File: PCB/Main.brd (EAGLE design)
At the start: 73 x 61 mm, 4 parts, among them U1 ESP32DEVKITC

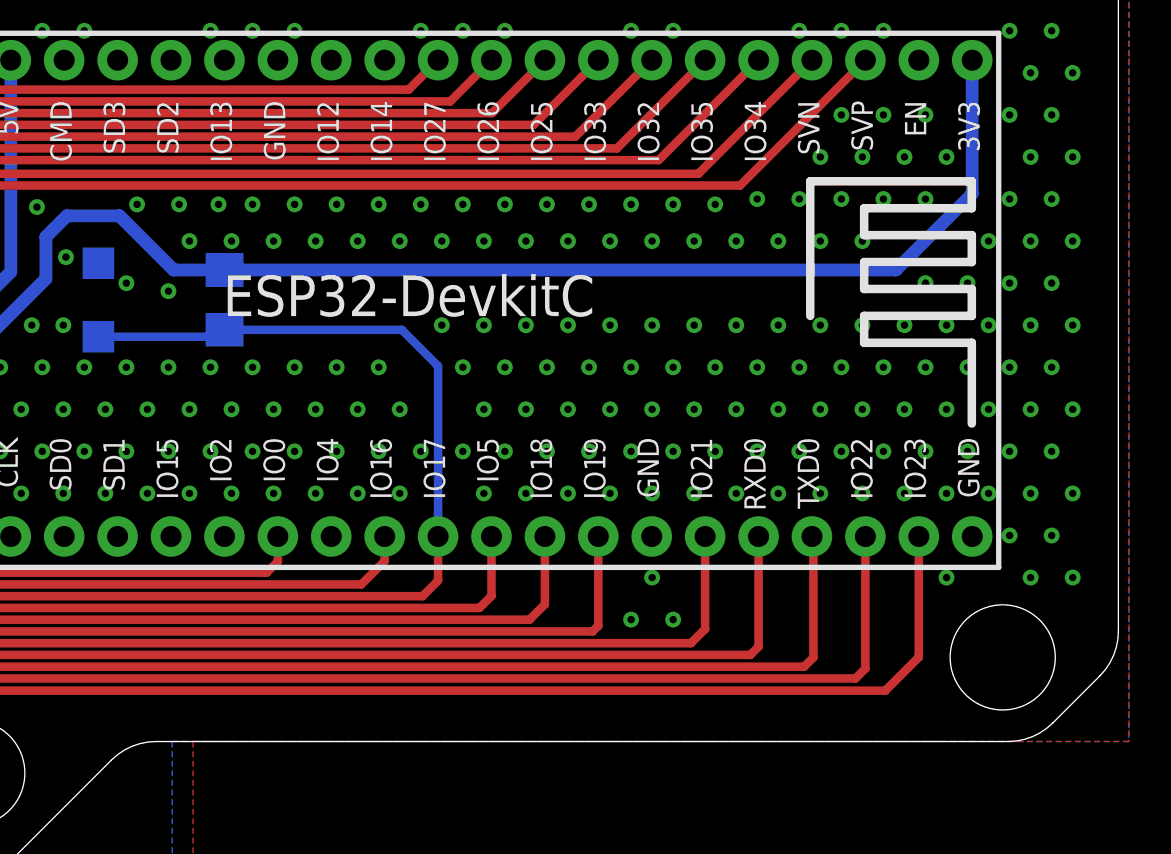
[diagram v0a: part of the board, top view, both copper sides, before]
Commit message: PCB Updates/New Additions
All existing PCBs had silkscreen updates and NES, Virtual Boy, PSX/PS2, Nintendo 64, Saturn have been added.
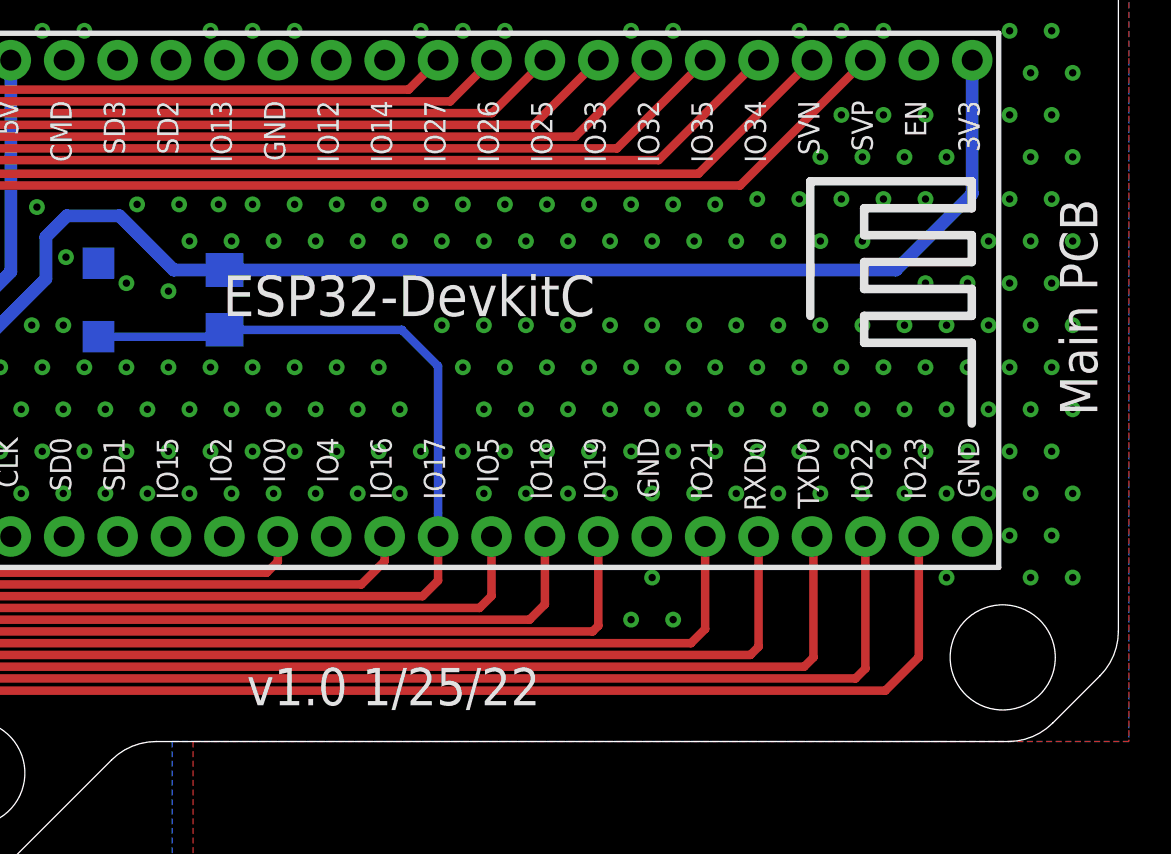
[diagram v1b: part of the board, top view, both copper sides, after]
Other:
- board text added: "Main PCB"
- board text added: "v1.0 1/25/22"
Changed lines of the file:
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@@
 <hole x="18.5" y="53" drill="5"/>
 <hole x="18.5" y="8" drill="5"/>
+<text x="72" y="25" size="1.778" layer="21" rot="R90">Main PCB</text>
+<text x="45.5" y="13" size="1.778" layer="21" rot="R180">v1.0 1/25/22</text>
 </plain>
 <attributes>

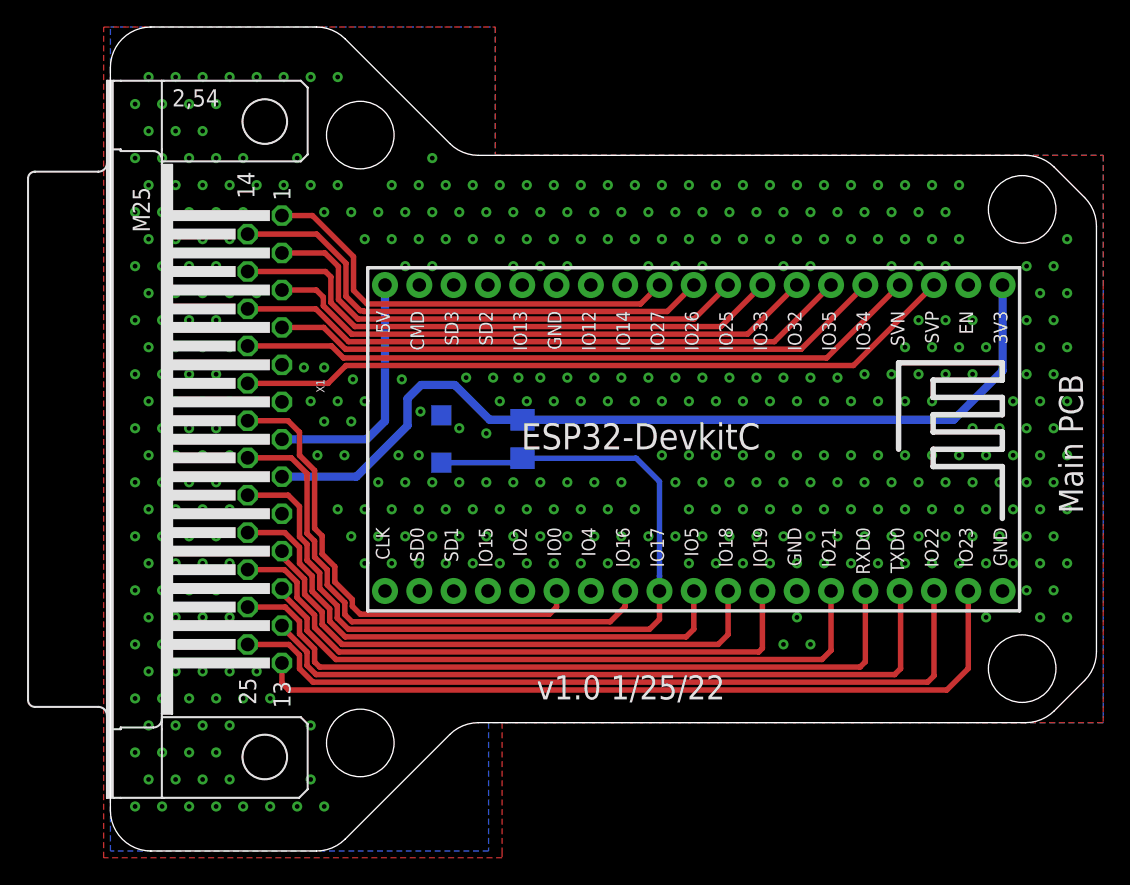
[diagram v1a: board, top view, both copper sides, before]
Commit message: Added exposed GND plane at DB25 anchors
All PCBs have been update to have exposed GND plane pads for the DB25 anchor points.

This resolves Issue 54
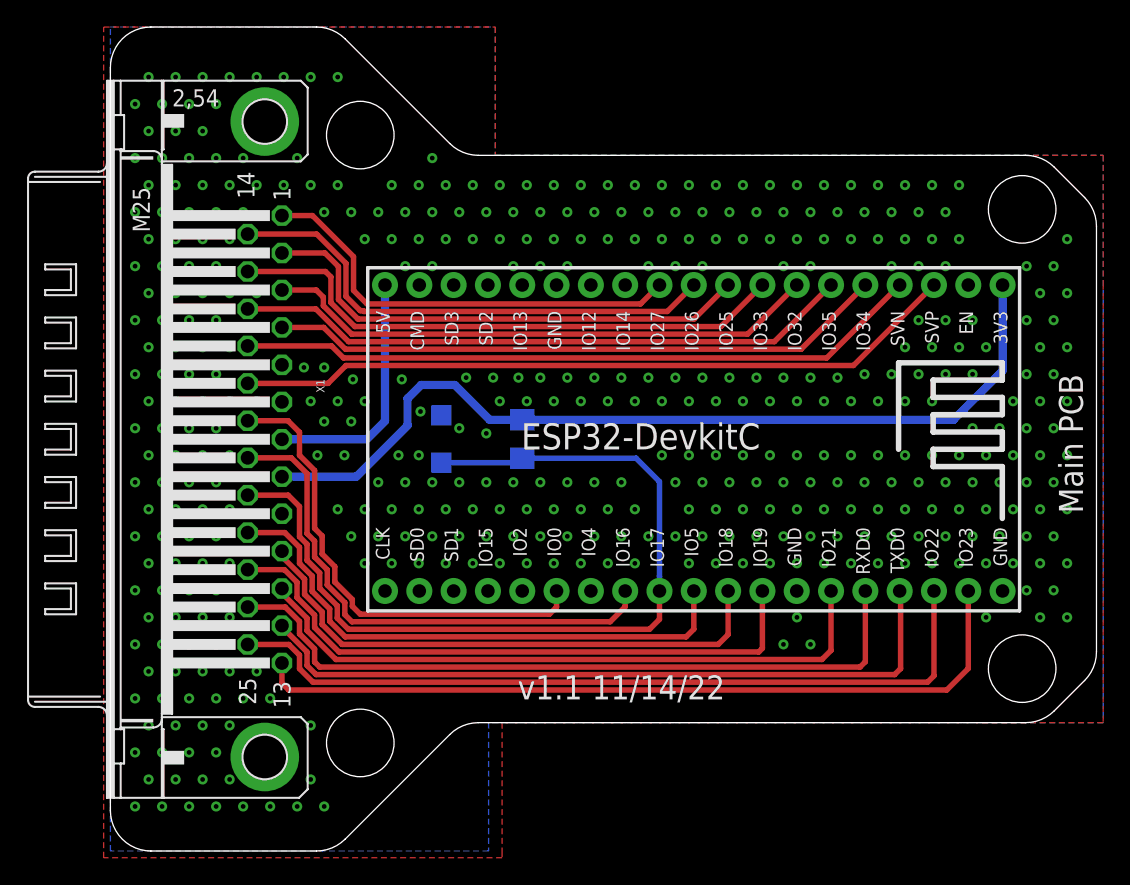
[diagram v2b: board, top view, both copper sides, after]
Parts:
- X1: device SparkFun-Retired:M25H -> SparkFun-Retired:M25HP
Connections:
- net GND: now also X1.G1, X1.G2
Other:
- board text added: "v1.1 11/14/22"
- board text removed: "v1.0 1/25/22"

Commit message: Retiring Main PCB
Retiring Original Main PCB design as the unit is thinner that the standard footprint.  This was causing  confusion.  The new main used to be Main Alt Wide version.  It is now the standard as it fits the standard ESP footprint.  The Thinner version has been moved to the retired folder in PCBs
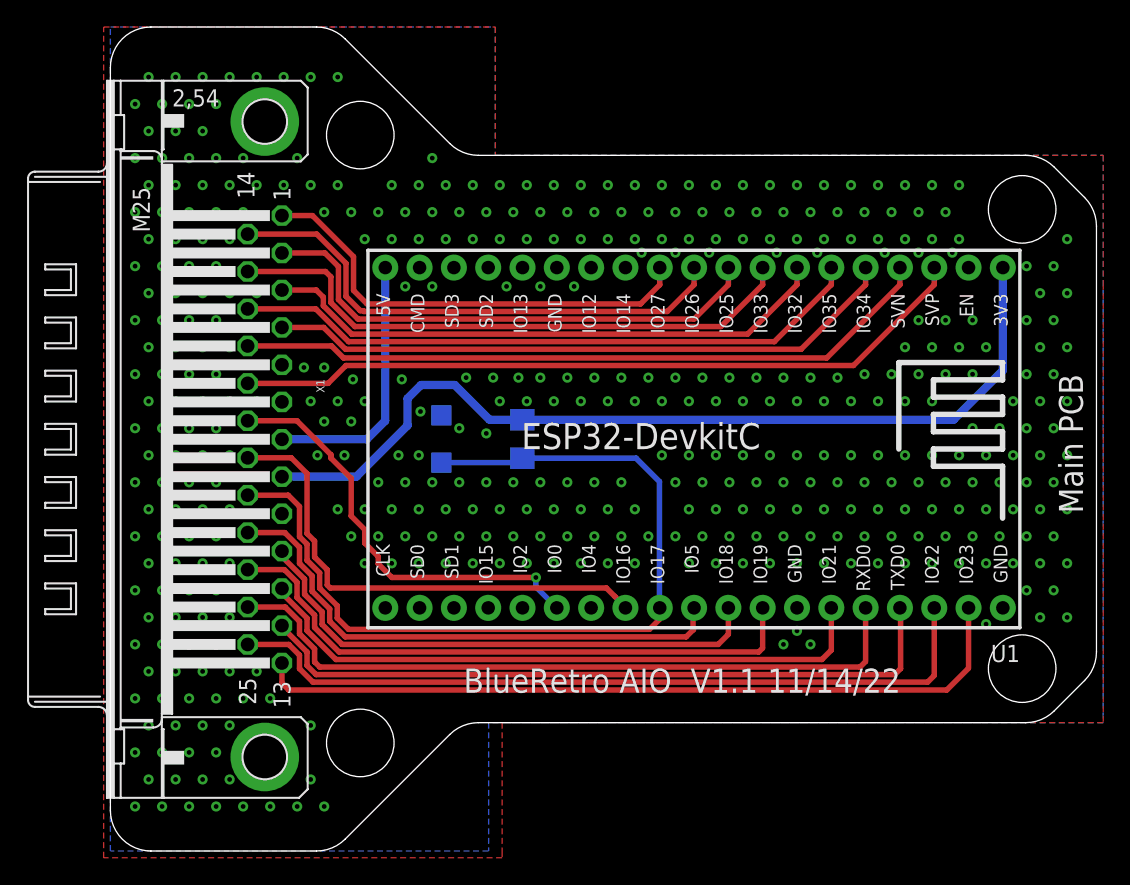
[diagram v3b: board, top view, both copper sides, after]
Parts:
- U1: device ESP32-DEVKITC:ESP32-DEVKITC -> ESP32-DEVKITC4:ESP32-DEVKITC
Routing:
- net IO0: track 35.5 -> 31.7 mm, vias 0 -> 1
- net IO16: track 39.1 -> 36.5 mm
- net 3V3IN: track 66.3 -> 67.6 mm
- net 5VIN: track 18.3 -> 19.6 mm
- net IO39: track 50.9 -> 52.2 mm
- net IO36: track 53.8 -> 55.1 mm
- net IO33: track 42.2 -> 43.5 mm
- net IO25: track 37.5 -> 38.8 mm
- net IO35: track 45.9 -> 47.2 mm
- net IO34: track 45.8 -> 47.1 mm
- net IO32: track 41.3 -> 42.6 mm
- net IO27: track 32.7 -> 34.0 mm
- net IO26: track 37.6 -> 38.9 mm
- net IO1: track 53.9 -> 52.6 mm
- net IO3: track 54.1 -> 52.8 mm
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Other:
- board text added: "BlueRetro AIO V1.1 11/14/22"
- board text removed: "v1.1 11/14/22"
